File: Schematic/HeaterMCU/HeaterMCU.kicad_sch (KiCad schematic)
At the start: 80 parts, among them J301 To µTracer, J302 Firmware, J303 To PSU Board, Q301 BSS138, Q302 BSS138, Q303 BSS138, Q304 BSS138, Q305 BSS138, SW301 RESET, U301 TPS54302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

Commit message: Added project pictures
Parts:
- R315: value 2.7kΩ -> 1.8kΩ
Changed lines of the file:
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@@
       (effects (font (size 1.27 1.27)) (justify left))
     )
-    (property "Value" "2.7kΩ" (id 1) (at 243.205 214.63 0)
+    (property "Value" "1.8kΩ" (id 1) (at 243.205 214.63 0)
       (effects (font (size 1.27 1.27)) (justify left))
     )
@@
     )
     (path "/e425db6b-d61f-4f19-b66d-560bcbed8498"
-      (reference "R315") (unit 1) (value "2.7kΩ") (footprint "Resistor_SMD:R_0603_1608Metric_Pad0.98x0.95mm_HandSolder")
+      (reference "R315") (unit 1) (value "1.8kΩ") (footprint "Resistor_SMD:R_0603_1608Metric_Pad0.98x0.95mm_HandSolder")
     )
     (path "/71307b9a-dec5-4cbe-ac19-b14e848626d4"

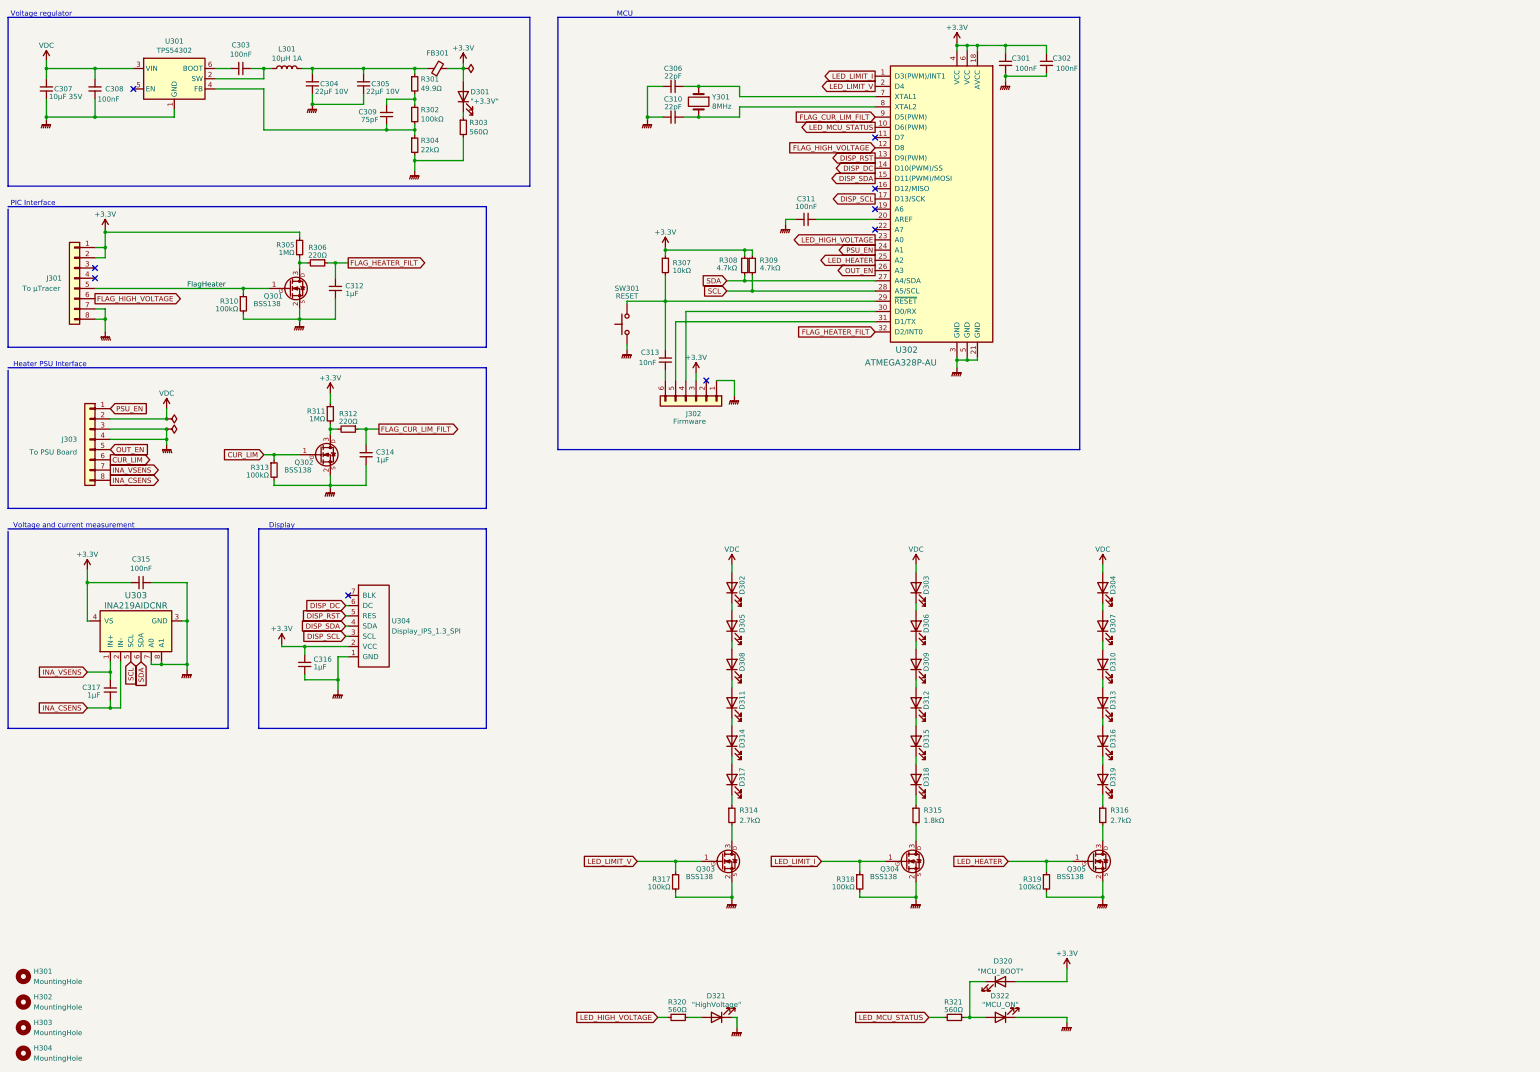
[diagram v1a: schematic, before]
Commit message: Added Front panel labels
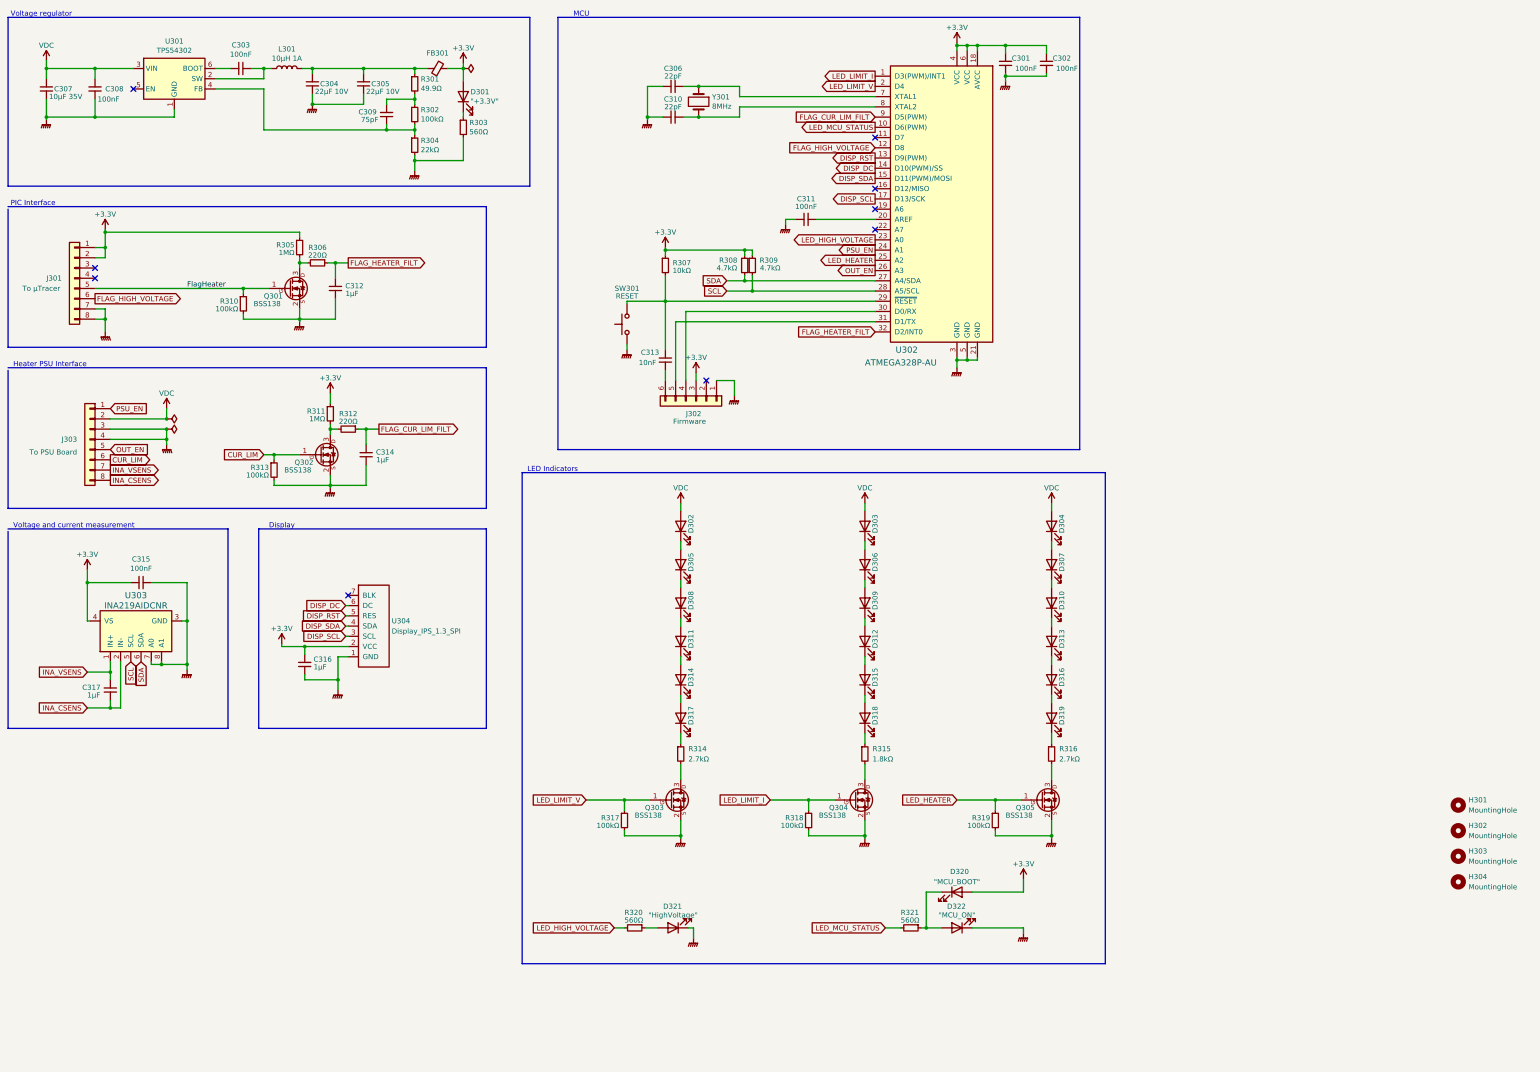
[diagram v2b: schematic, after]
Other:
- note added: "LED Indicators"
- moved on the sheet: D302, D303, D304, D305, D306, D307, D308, D309, D310, D311, D312, D313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

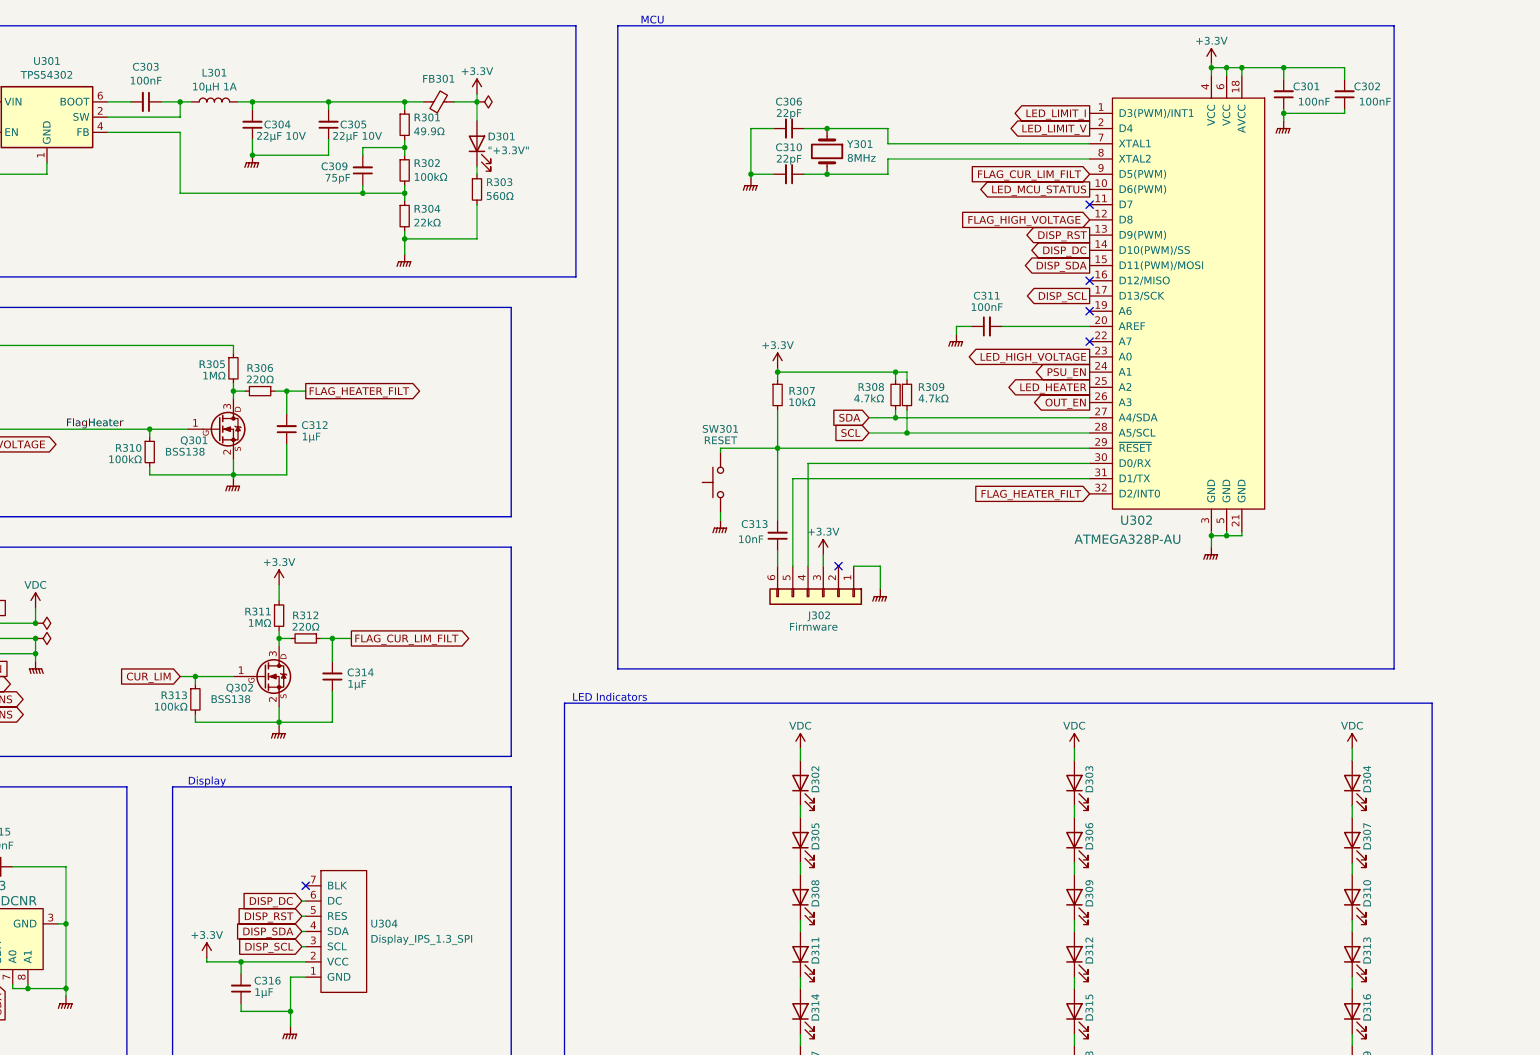
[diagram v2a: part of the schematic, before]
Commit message: Added BOM (bill of materials)
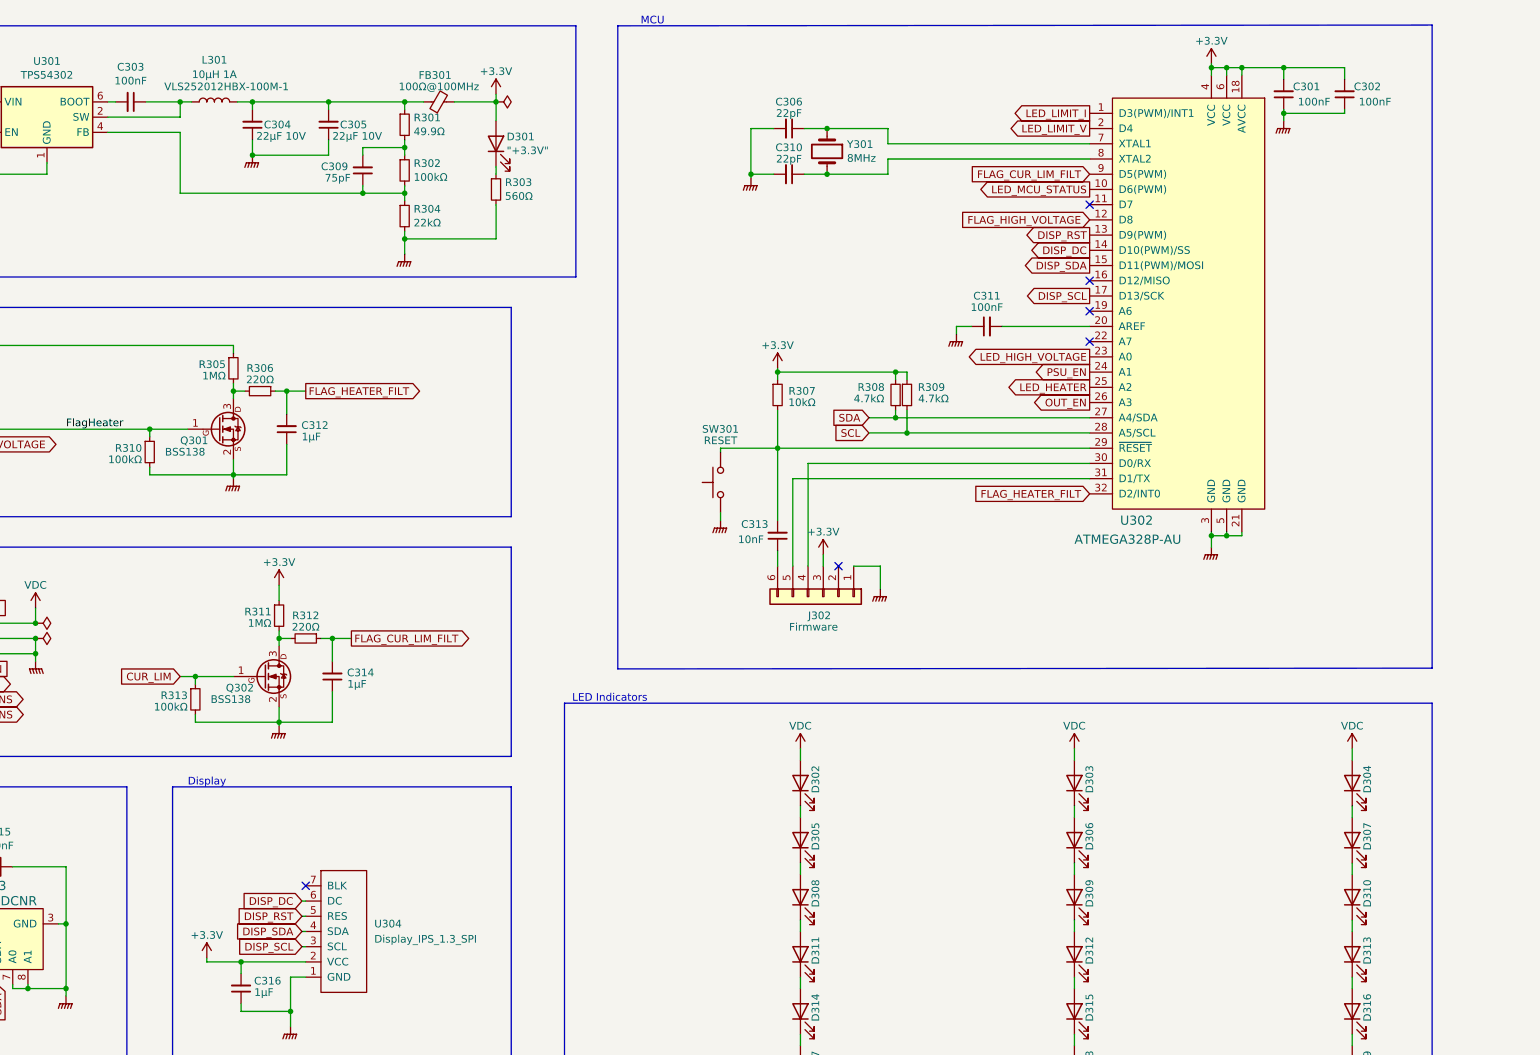
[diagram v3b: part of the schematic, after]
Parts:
- FB301: value FerriteBead_Small -> 100Ω@100MHz
- L301: Comments (none) -> VLS252012HBX-100M-1
- U304: Comments (none) -> https://www.buydisplay.com/1-3-inch-tft-ips-lcd-display-mod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
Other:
- moved on the sheet: C303, D301, R303
